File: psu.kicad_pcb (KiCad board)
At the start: 2 copper layers, 55 parts, among them J1 Screw_Terminal_01x02, J2 Barrel_Jack, J3 Binding posts, SW1 SW_SP4T, SW2 SW_SP4T, SW3 Lever toggle, U1 LM4040DBZ-2.5, U2 LT3081, U3 LM393, U4 LM334M

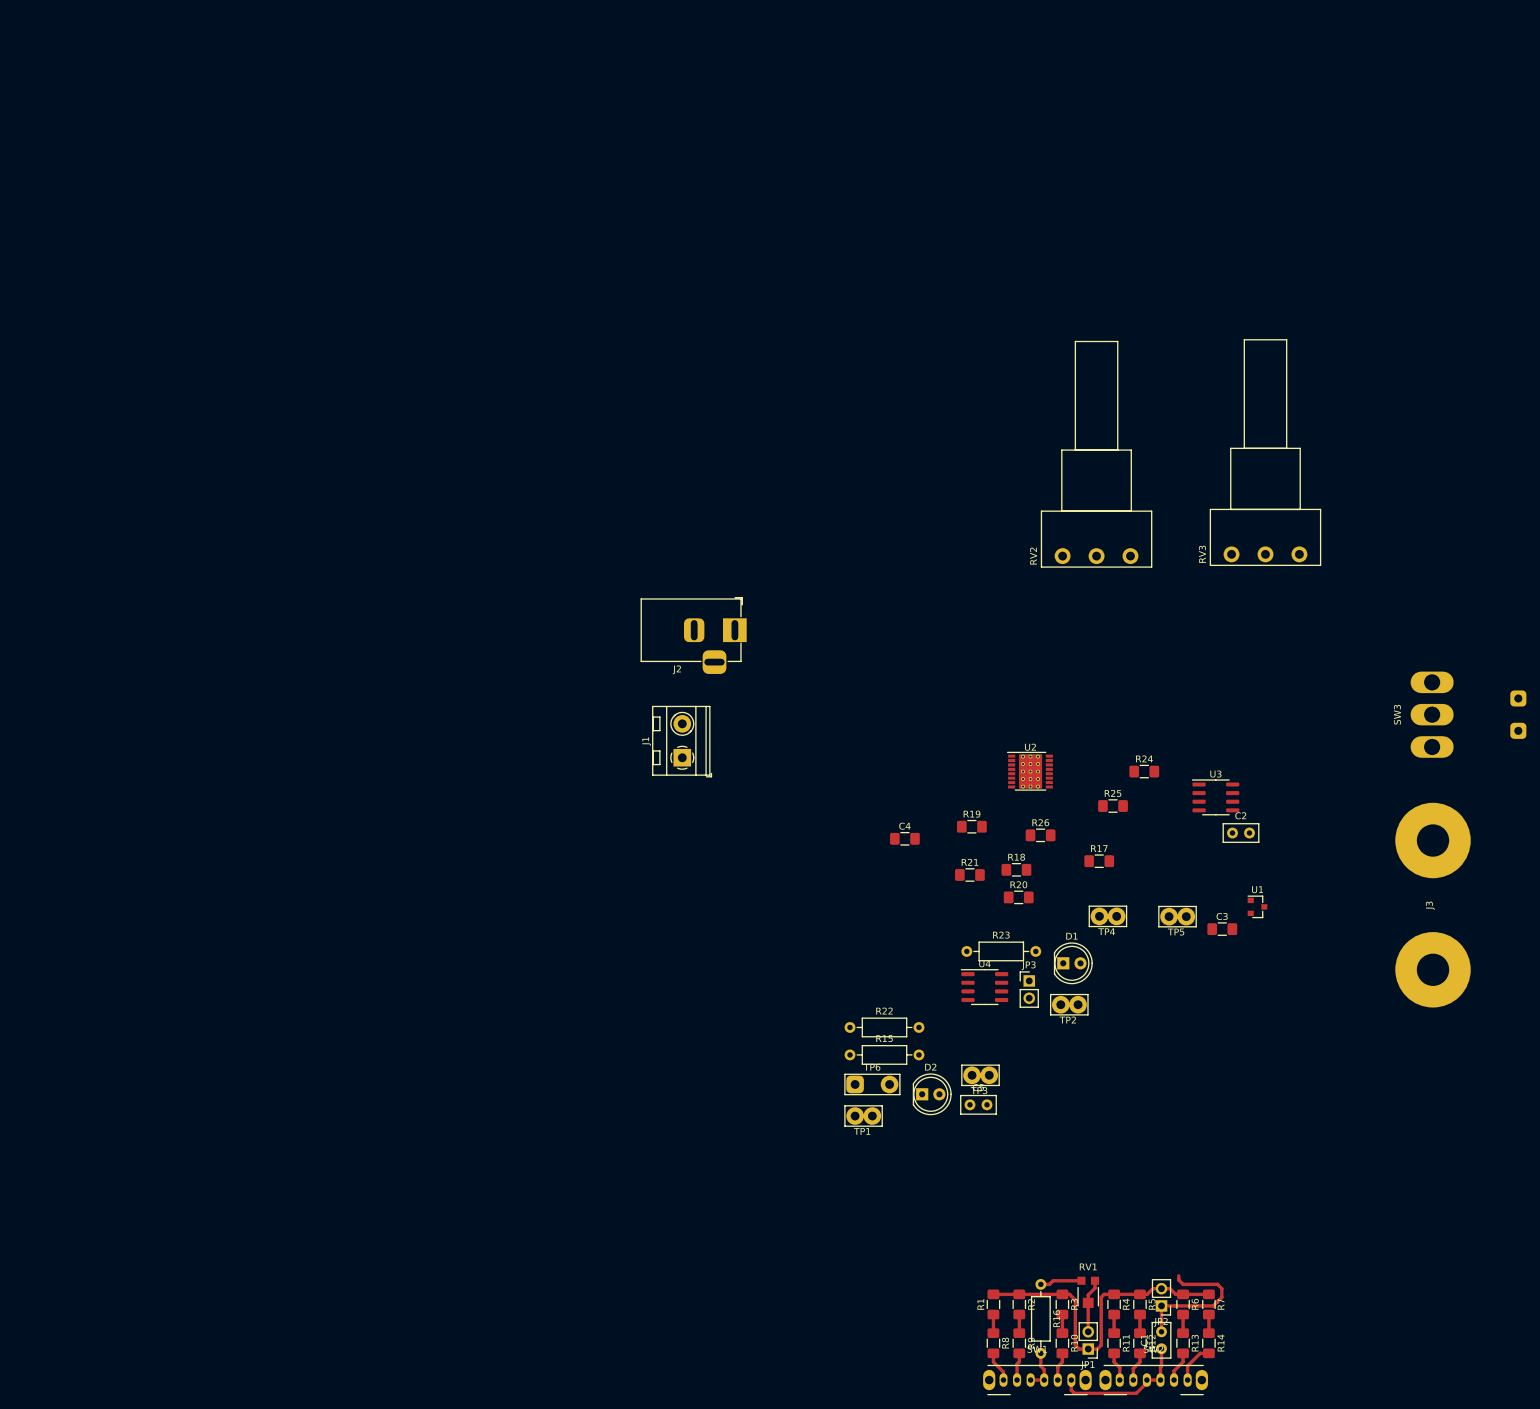
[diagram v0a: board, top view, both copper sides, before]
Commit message: Minor schematic tweaks; more routing
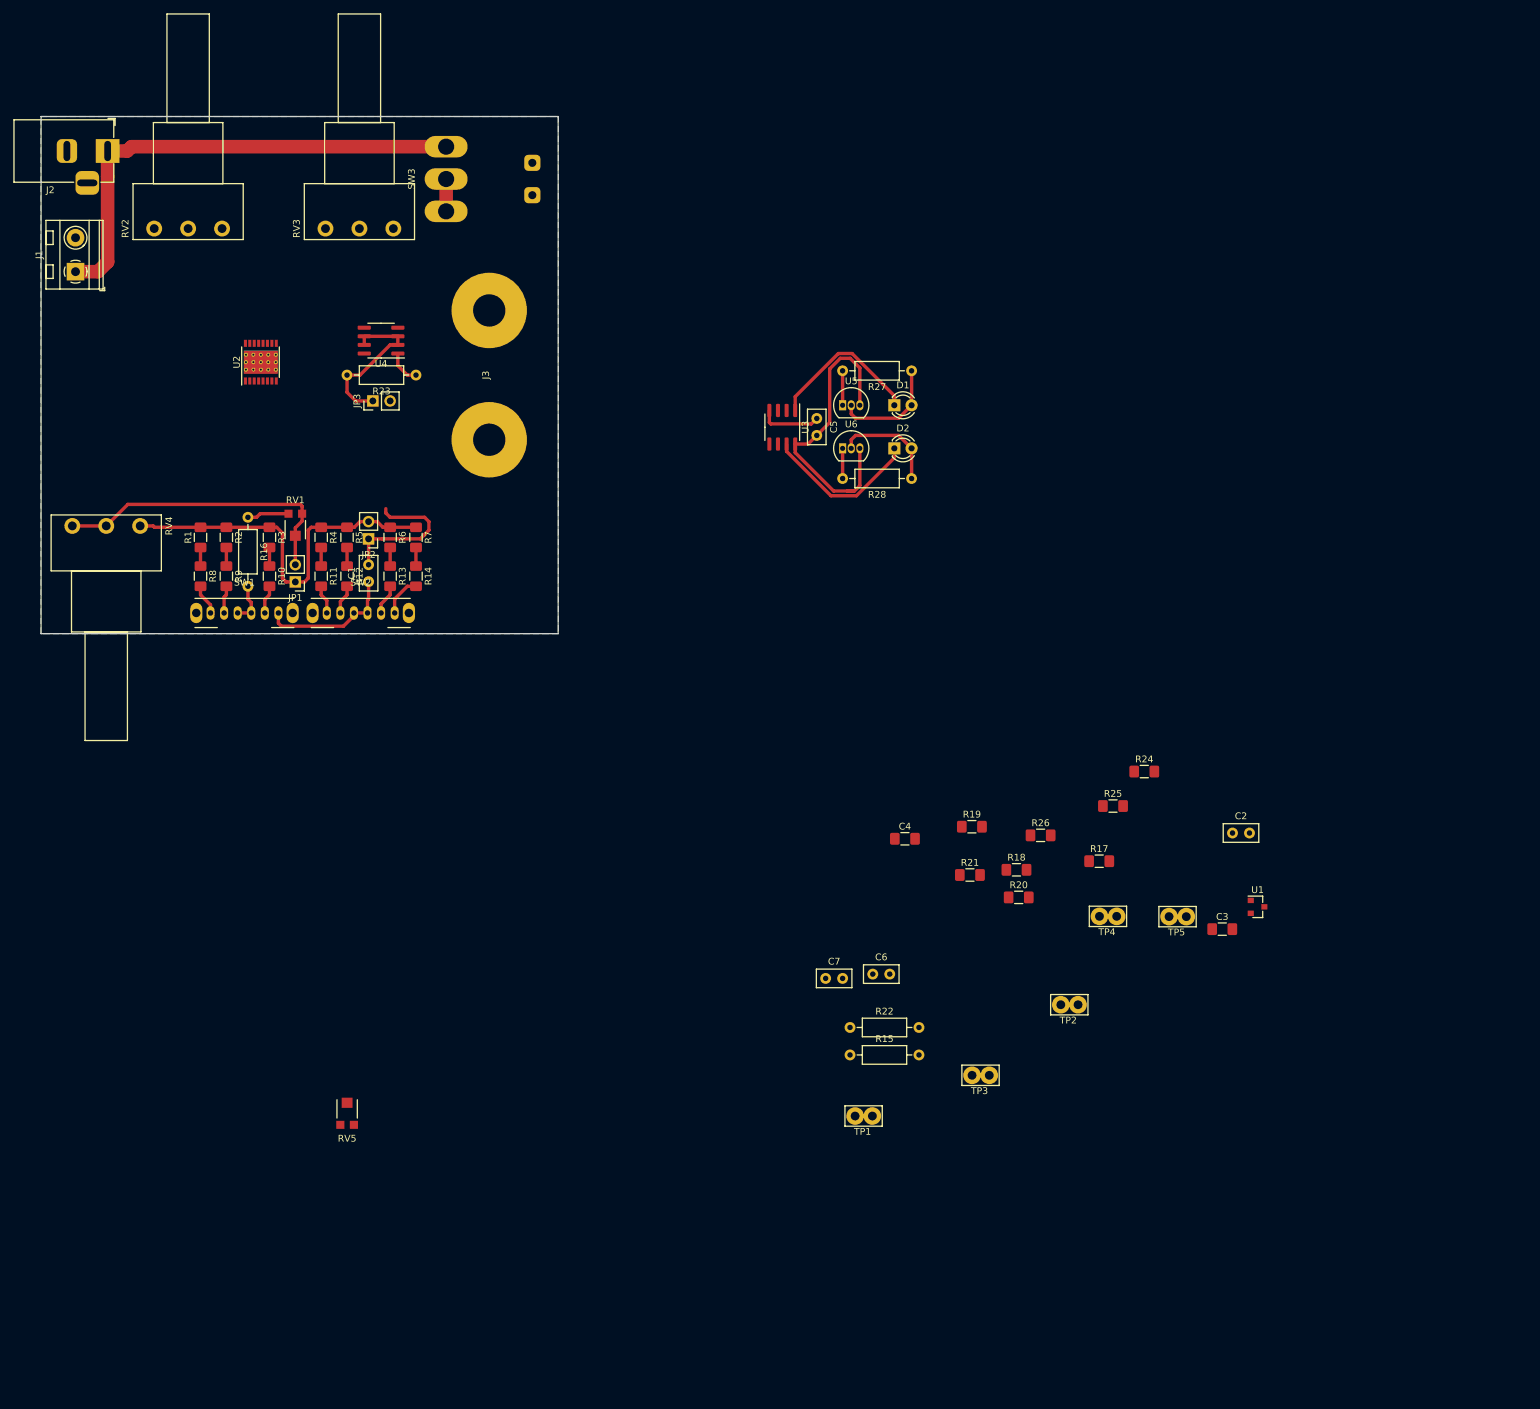
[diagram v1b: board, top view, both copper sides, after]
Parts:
- removed TP6: Vout test, TestPoint:TestPoint_2Pads_Pitch5.08mm_Drill1.3mm
- added C6: 0u1, Capacitor_THT:C_Disc_D5.0mm_W2.5mm_P2.50mm, F.Cu at (122.6, 126.4)
- added C7: 0u1, Capacitor_THT:C_Disc_D5.0mm_W2.5mm_P2.50mm, F.Cu at (115.6, 127.0)
- added R27: 100R, Resistor_THT:R_Axial_DIN0207_L6.3mm_D2.5mm_P10.16mm_Horizontal, F.Cu at (128.3, 37.5)
- added R28: 100R, Resistor_THT:R_Axial_DIN0207_L6.3mm_D2.5mm_P10.16mm_Horizontal, F.Cu at (128.3, 53.3)
- added RV4: 1k, Potentiometer_THT:Potentiometer_Piher_PC-16_Single_Horizontal, F.Cu at (4.61, 60.3)
- added RV5: 500k, psu-foot:Trim_pot_Bourns_TC33X-2-101E, F.Cu at (45.1, 146.8)
- added U5: LM317L_TO92, Package_TO_SOT_THT:TO-92_Inline, F.Cu at (118.1, 42.5)
- added U6: LM317L_TO92, Package_TO_SOT_THT:TO-92_Inline, F.Cu at (118.1, 48.9)
- D1, D2: footprint LED_THT:LED_D5.0mm -> LED_THT:LED_D3.0mm
- JP1: value Minimum limit -> Min Lim
- moved SW3 165.3 mm to (59.7, 9.21)
- moved JP1 162.6 mm to (37.5, 68.6)
- moved JP2 162.6 mm to (48.3, 62.2)
- moved C1 162.6 mm to (48.3, 68.5)
- moved R1 162.6 mm to (23.5, 62.0)
- moved R10 162.6 mm to (33.7, 67.7)
- moved R11 162.6 mm to (41.3, 67.7)
- moved R12 162.6 mm to (45.1, 67.7)
- moved R13 162.6 mm to (51.4, 67.7)
- moved R14 162.6 mm to (55.2, 67.7)
- moved R16 162.6 mm to (30.5, 59.1)
- moved R2 162.6 mm to (27.3, 62.0)
- moved R3 162.6 mm to (33.7, 62.0)
- moved R4 162.6 mm to (41.3, 62.0)
- moved R5 162.6 mm to (45.1, 62.0)
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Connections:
- D1 pad 2: Vin -> Net-(D1-Pad2)
- D2 pad 2: Vin -> Net-(D2-Pad2)
- U2 pad 17: (no net) -> Vout
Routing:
- net Net-(J1-Pad1): track 0.00 -> 71.8 mm
- net Vin: track 0.00 -> 49.8 mm
- net Vout: track 7.93 -> 44.3 mm
- net Net-(JP3-Pad1): track 0.00 -> 23.7 mm
- net Net-(D2-Pad1): track 0.00 -> 23.4 mm
- net Net-(D1-Pad1): track 0.00 -> 23.2 mm
- net Net-(D1-Pad2): track 0.00 -> 16.3 mm
- net Net-(D2-Pad2): track 0.00 -> 15.7 mm
- net GND: track 0.00 -> 9.18 mm
- net Net-(JP1-Pad1): track 47.2 -> 56.1 mm
- net Net-(R27-Pad2): track 0.00 -> 5.08 mm
- net Net-(R23-Pad1): track 0.00 -> 5.02 mm
- net Net-(R28-Pad2): track 0.00 -> 4.45 mm
- added copper zone on B.Cu, net GND
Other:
- board outline added: 76.2 x 76.2 mm

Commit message: Mostly routed
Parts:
- added JP4: Guard, psu-foot:Guard_Jumper, F.Cu at (145.3, 108.2)
- added JP5: Guard, psu-foot:Guard_Jumper, F.Cu at (147.6, 108.2)
- moved JP3 146.1 mm to (164.7, 130.9)
- moved R23 146.1 mm to (171.1, 127.1)
- moved U4 146.1 mm to (165.9, 122.0)
- moved U2 128.4 mm to (145.0, 97.8)
- moved C1 115.7 mm to (147.3, 128.2)
- moved J1 115.7 mm to (104.1, 82.5)
- moved J2 115.7 mm to (108.9, 64.8)
- moved JP1 115.7 mm to (136.5, 128.3)
- moved JP2 115.7 mm to (147.3, 121.9)
- moved R1 115.7 mm to (122.6, 121.7)
- moved R10 115.7 mm to (132.7, 127.4)
- moved R11 115.7 mm to (140.3, 127.4)
- moved R12 115.7 mm to (144.1, 127.4)
- moved R13 115.7 mm to (150.5, 127.4)
- moved R14 115.7 mm to (154.3, 127.4)
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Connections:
- U2 pad 6: Net-(C1-Pad2) -> Net-(JP4-Pad1)
- U2 pad 7: Net-(C2-Pad2) -> Net-(JP5-Pad1)
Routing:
- net Net-(RV2-Pad2): track 0.00 -> 74.2 mm
- net GND: track 9.18 -> 79.0 mm, vias 0 -> 40
- net Vout: track 44.3 -> 84.1 mm, vias 0 -> 1
- net Vin: track 49.8 -> 83.5 mm
- net Net-(R15-Pad1): track 0.00 -> 12.4 mm
- net Net-(R21-Pad1): track 0.00 -> 9.06 mm
- net Net-(R19-Pad1): track 0.00 -> 8.50 mm
- net Iout: track 0.00 -> 7.73 mm
- net Net-(R17-Pad2): track 0.00 -> 7.04 mm
- net Net-(R22-Pad1): track 0.00 -> 4.71 mm
- net TEMP: track 0.00 -> 3.92 mm
- net Net-(JP5-Pad1): track 0.00 -> 2.94 mm
- net Net-(JP4-Pad1): track 0.00 -> 2.86 mm
- net Net-(D1-Pad1): track 23.2 -> 25.0 mm
- net (no net): vias 0 -> 74
- added copper zone on F.Cu, net Vout
- removed copper zone on B.Cu, net GND

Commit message: More routing; some issues
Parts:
- added C8: 0u1, Capacitor_THT:C_Disc_D5.0mm_W2.5mm_P2.50mm, F.Cu at (183.7, 107.8)
- added REF**: MountingHole_3.2mm_M3, MountingHole:MountingHole_3.2mm_M3, F.Cu at (171.4, 63.5)
- added REF**: MountingHole_3.2mm_M3, MountingHole:MountingHole_3.2mm_M3, F.Cu at (171.4, 132.1)
- added REF**: MountingHole_3.2mm_M3, MountingHole:MountingHole_3.2mm_M3, F.Cu at (102.9, 132.1)
- added REF**: MountingHole_3.2mm_M3, MountingHole:MountingHole_3.2mm_M3, F.Cu at (102.9, 63.5)
- moved RV5 17.8 mm to (115.3, 116.0), turned to 90 degrees
- moved C2 16.3 mm to (153.1, 114.6), turned to 180 degrees
- moved R28 12.6 mm to (111.8, 102.1), turned to 180 degrees
- moved R21 11.7 mm to (115.6, 111.8), turned to 180 degrees
- moved R27 11.4 mm to (111.8, 105.4), turned to 180 degrees
- moved J2 8.92 mm to (109.6, 73.7)
- moved C4 8.85 mm to (139.7, 88.6), turned to 90 degrees
- moved J1 6.35 mm to (104.1, 88.9)
- moved U5 5.92 mm to (108.7, 110.5), turned to 0 degrees
- moved D1 5.68 mm to (101.6, 110.5), turned to 0 degrees
- moved R17 5.15 mm to (121.3, 108.6), turned to 180 degrees
- moved U1 4.89 mm to (114.6, 85.5)
- moved SW3 4.62 mm to (160.0, 73.3)
- moved R18 4.40 mm to (115.6, 108.6), turned to 180 degrees
- moved R16 3.81 mm to (129.5, 114.9)
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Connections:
- R27 pad 1: Net-(D1-Pad2) -> Net-(R27-Pad1)
- R27 pad 2: Net-(R27-Pad2) -> Net-(D1-Pad2)
- R28 pad 1: Net-(D2-Pad2) -> Net-(R28-Pad1)
- R28 pad 2: Net-(R28-Pad2) -> Net-(D2-Pad2)
- U5 pad 1: Net-(R27-Pad2) -> Net-(D1-Pad2)
- U5 pad 2: Net-(D1-Pad2) -> Net-(R27-Pad1)
- U6 pad 1: Net-(R28-Pad2) -> Net-(D2-Pad2)
- U6 pad 2: Net-(D2-Pad2) -> Net-(R28-Pad1)
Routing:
- net Net-(C2-Pad2): track 0.00 -> 68.8 mm
- net Net-(RV2-Pad2): track 74.2 -> 38.8 mm
- net Vout: track 84.1 -> 110.4 mm, vias 1 -> 15
- net Vin: track 83.5 -> 66.4 mm
- net Net-(R28-Pad1): track 0.00 -> 6.07 mm
- net Net-(R27-Pad1): track 0.00 -> 5.82 mm
- net Net-(R21-Pad1): track 9.06 -> 14.7 mm
- net Net-(C1-Pad2): track 22.0 -> 27.2 mm
- net Net-(R27-Pad2): track 5.08 -> 0.00 mm
- net Net-(D1-Pad2): track 16.3 -> 11.6 mm
- net Net-(R28-Pad2): track 4.45 -> 0.00 mm
- net Net-(D2-Pad2): track 15.7 -> 11.3 mm
- net GND: track 79.0 -> 76.1 mm, vias 40 -> 50
- net Net-(JP1-Pad1): track 56.1 -> 53.7 mm
- net Net-(R15-Pad1): track 12.4 -> 14.8 mm
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- added copper zone on B.Cu, net GND
- added copper zone on B.Cu, net Vout

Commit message: It's all connected man
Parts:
- removed the REF** at (171.4, 63.5)
- removed the REF** at (171.4, 132.1)
- removed the REF** at (102.9, 132.1)
- removed the REF** at (102.9, 63.5)
- removed TP3: Iout, TestPoint:TestPoint_Bridge_Pitch2.54mm_Drill1.3mm
- removed TP4: Temp, TestPoint:TestPoint_Bridge_Pitch2.54mm_Drill1.3mm
- added REF**: MountingHole_3.2mm_M3, Mounting_Holes:MountingHole_3.2mm_M3, F.Cu at (102.9, 132.1)
- added REF**: MountingHole_3.2mm_M3, Mounting_Holes:MountingHole_3.2mm_M3, F.Cu at (171.4, 132.1)
- added REF**: MountingHole_3.2mm_M3, Mounting_Holes:MountingHole_3.2mm_M3, F.Cu at (171.4, 63.5)
- added REF**: MountingHole_3.2mm_M3, Mounting_Holes:MountingHole_3.2mm_M3, F.Cu at (102.9, 63.5)
- moved TP1 82.4 mm to (157.5, 63.5)
- moved TP5 77.6 mm to (162.6, 132.7)
- moved C3 61.5 mm to (132.9, 79.4)
- moved C8 61.1 mm to (131.4, 76.1)
- moved TP2 50.2 mm to (170.8, 117.6), turned to 270 degrees
- moved C4 35.7 mm to (165.1, 63.5)
- moved C6 19.7 mm to (155.2, 80.0)
- moved R22 16.6 mm to (125.7, 82.5), turned to 0 degrees
- moved C7 10.8 mm to (140.0, 80.0)
- moved R24 8.26 mm to (147.6, 81.1)
- moved R25 8.26 mm to (151.4, 81.1)
- moved R26 3.18 mm to (143.8, 81.1)
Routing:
- net Vout: track 110.4 -> 223.0 mm, vias 15 -> 29
- net Vin: track 66.4 -> 151.9 mm, vias 0 -> 4
- net TEMP: track 3.92 -> 21.8 mm, vias 0 -> 2
- net Net-(R22-Pad1): track 4.71 -> 20.7 mm
- net Iout: track 7.73 -> 23.3 mm, vias 0 -> 2
- net Net-(R15-Pad1): track 14.8 -> 10.8 mm
- net GND: track 76.1 -> 75.8 mm, vias 50 -> 20
- net (no net): vias 63 -> 0

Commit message: Tweaks
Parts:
- moved J3 1.27 mm to (166.4, 97.8)
- moved JP4 1.02 mm to (145.3, 109.2)
- moved JP5 1.02 mm to (147.6, 109.2)
- moved RV4 0.54 mm to (107.3, 120.2)
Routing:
- net Vout: track 223.0 -> 303.5 mm, vias 29 -> 12
- net TEMP: track 21.8 -> 24.8 mm
- net Vin: track 151.9 -> 150.8 mm
- net Net-(C2-Pad2): track 68.8 -> 69.4 mm
- net Net-(JP1-Pad1): track 53.7 -> 53.2 mm

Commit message: Silkscreen overhaul
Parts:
- moved J1 1.27 mm to (105.4, 88.9)
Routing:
- net Vout: track 303.5 -> 308.4 mm, vias 12 -> 11
- net Vin: track 150.8 -> 151.6 mm
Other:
- board text added: "(I lim)"
- board text added: "+"
- board text added: "-"
- board text added: "1"
- board text added: "10"
- board text added: "100"
- board text added: "2.5"
- board text added: "25"
- board text added: "5"
- board text added: "50"
- board text added: "Coarse"
- board text added: "Error Offset"
- board text added: "Fine"
- board text added: "GND"
- board text added: "Hot"
- board text added: "I (mA)"
- board text added: "Iout"
- board text added: "LM317"
- board text added: "LM334"
- board text added: "LM393"
- board text added: "LM4040 (2.5V)"
- board text added: "LT3081"
- board text added: "Load Offset"
- board text added: "Min Lim"
- board text added: "No Limit"
- board text added: "OCP"
- board text added: "Temp"
- board text added: "Vin"
- board text added: "Vout"
- board text added: "Vout Adjust"
- board text added: "Vout Error"
- board text added: "a"
- board text added: "b"
- board text added: "c"
- board text added: "d"
